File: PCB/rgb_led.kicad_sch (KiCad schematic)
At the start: 3 parts

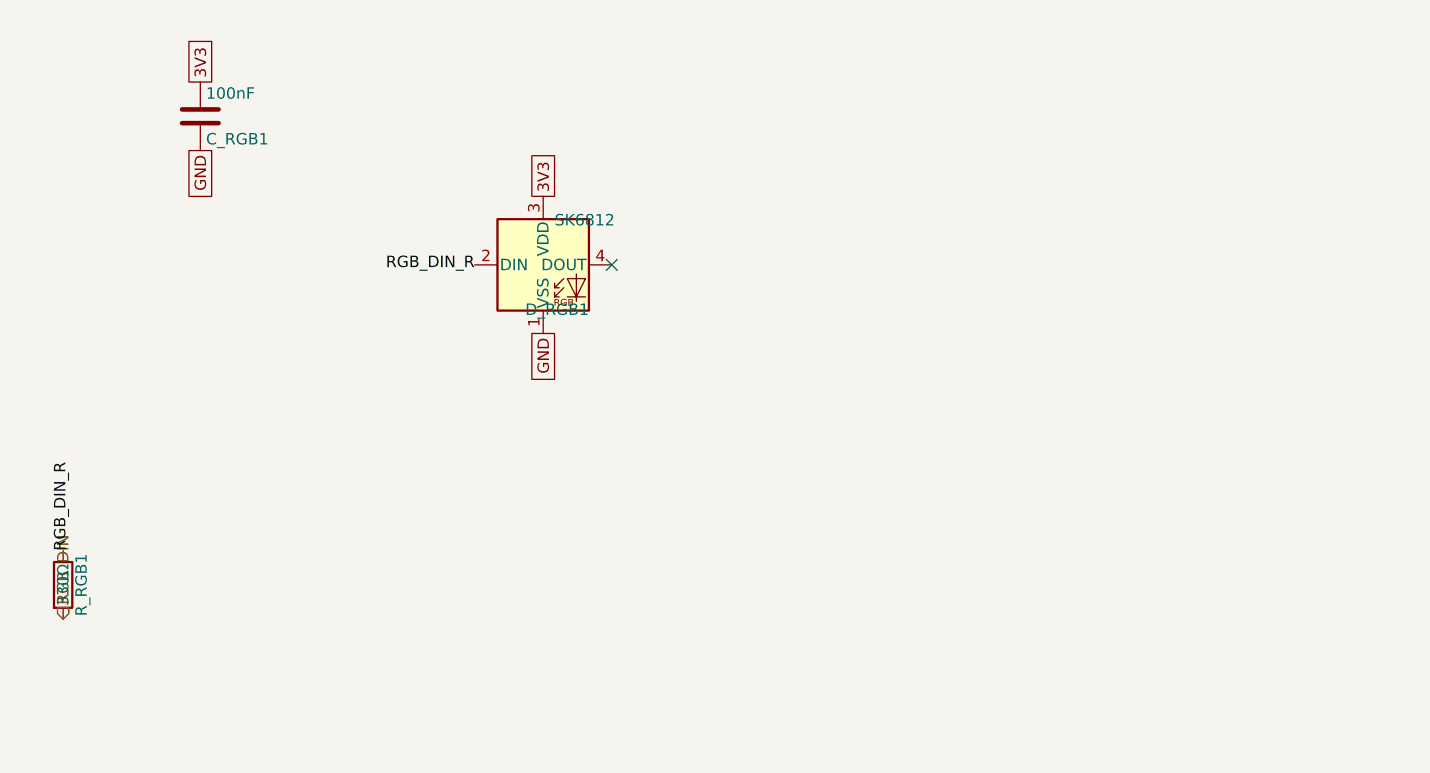
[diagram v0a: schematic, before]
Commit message: refactor: updated gulikit footprint
This updates the gulikit thumbstick footprint to be accurate.
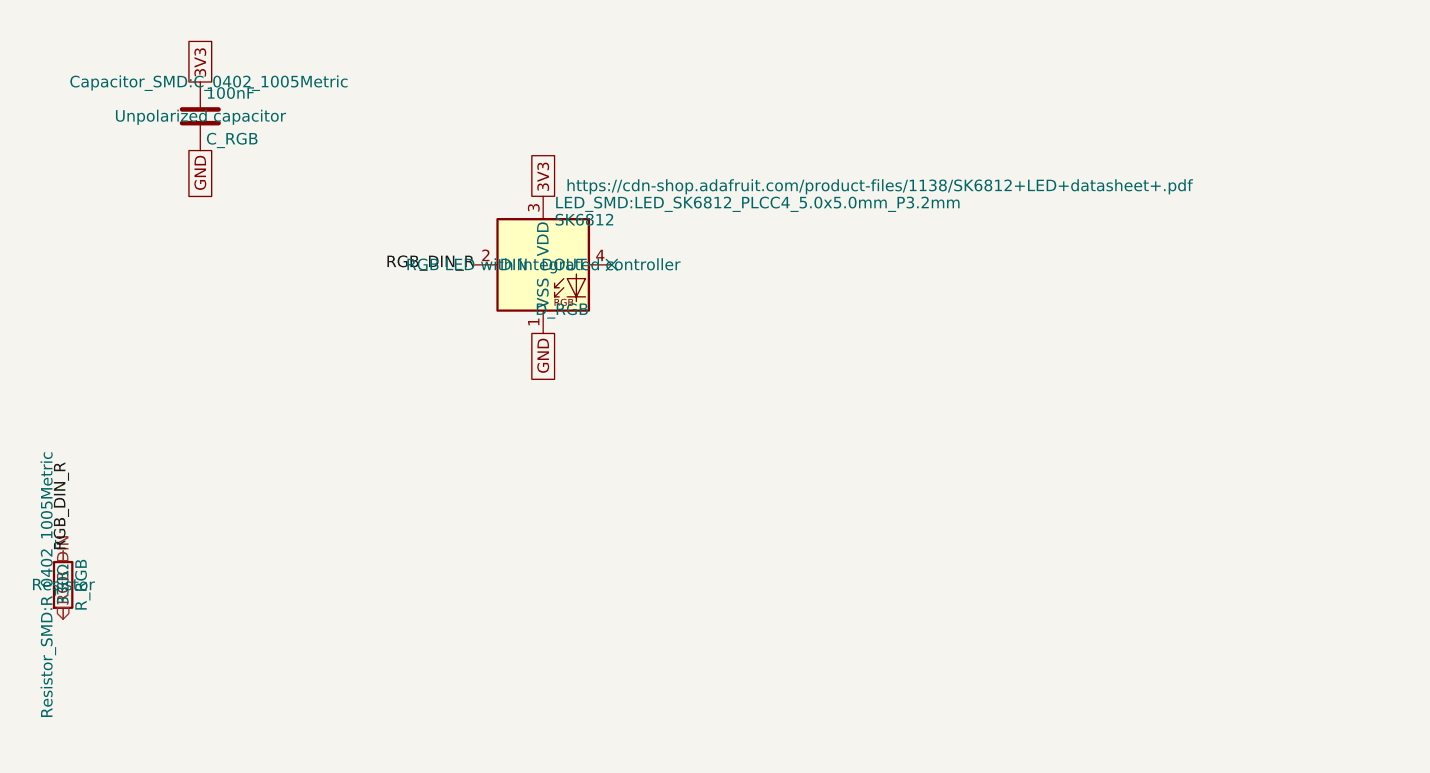
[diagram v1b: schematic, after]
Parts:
- removed C_RGB1: 100nF, Capacitor_SMD:C_0402_1005Metric, symbol Device:C
- removed D_RGB1: SK6812, LED_SMD:LED_SK6812_PLCC4_5.0x5.0mm_P3.2mm, symbol LED:SK6812
- removed R_RGB1: 330Ω, Resistor_SMD:R_0402_1005Metric, symbol Device:R
- added C_RGB: 100nF, Capacitor_SMD:C_0402_1005Metric, symbol Device:C
- added D_RGB: SK6812, LED_SMD:LED_SK6812_PLCC4_5.0x5.0mm_P3.2mm, symbol LED:SK6812
- added R_RGB: 330Ω, Resistor_SMD:R_0402_1005Metric, symbol Device:R
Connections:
- net 3V3: now also C_RGB.1, D_RGB.3 (VDD)
- net GND: now also C_RGB.2, D_RGB.1 (VSS)
- net RGB_DIN: now also R_RGB.2
- net RGB_DIN_R: now also D_RGB.2 (DIN), R_RGB.1
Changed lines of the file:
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@@
 		(dnp no)
 		(fields_autoplaced yes)
-		(property "Reference" "D_RGB1"
+		(property "Reference" "D_RGB"
 			(at 180.34 100.965 0)
 			(show_name no)
@@
 		(property "Footprint" "LED_SMD:LED_SK6812_PLCC4_5.0x5.0mm_P3.2mm"
 			(at 176.53 87.63 0)
-			(hide yes)
 			(show_name no)
 			(do_not_autoplace no)
@@
 		(property "Datasheet" "https://cdn-shop.adafruit.com/product-files/1138/SK6812+LED+datasheet+.pdf"
 			(at 177.8 85.725 0)
-			(hide yes)
 			(show_name no)
 			(do_not_autoplace no)
@@
 		(property "Description" "RGB LED with integrated controller"
 			(at 175.26 95.25 0)
-			(hide yes)
 			(show_name no)
 			(do_not_autoplace no)
@@
 		)
 		(instances
-			(project "snips_controller"
-				(path "/868f8289-8434-4465-b2f4-2accc5e40bab/735d8d44-e064-4356-9d02-a40b0078b674"
-					(reference "D_RGB1")
+			(project ""
+				(path "/d0f5b7d7-b2b6-4492-958c-e60265d3c6b4/e8a027f5-b0c3-4230-8e98-ef586f634016"
+					(reference "D_RGB")
 					(unit 1)
 				)
@@
 		(dnp no)
 		(fields_autoplaced yes)
-		(property "Reference" "C_RGB1"
+		(property "Reference" "C_RGB"
 			(at 137.795 81.28 0)
 			(show_name no)
@@
 		(property "Footprint" "Capacitor_SMD:C_0402_1005Metric"
 			(at 138.1252 74.93 0)
-			(hide yes)
 			(show_name no)
 			(do_not_autoplace no)
@@
 		(property "Datasheet" ""
 			(at 137.16 78.74 0)
-			(hide yes)
 			(show_name no)
 			(do_not_autoplace no)
@@
 		(property "Description" "Unpolarized capacitor"
 			(at 137.16 78.74 0)
-			(hide yes)
 			(show_name no)
 			(do_not_autoplace no)
@@
 		)
 		(instances
-			(project "snips_controller"
-				(path "/868f8289-8434-4465-b2f4-2accc5e40bab/735d8d44-e064-4356-9d02-a40b0078b674"
-					(reference "C_RGB1")
+			(project ""
+				(path "/d0f5b7d7-b2b6-4492-958c-e60265d3c6b4/e8a027f5-b0c3-4230-8e98-ef586f634016"
+					(reference "C_RGB")
 					(unit 1)
 				)
@@
 		(dnp no)
 		(fields_autoplaced yes)
-		(property "Reference" "R_RGB1"
+		(property "Reference" "R_RGB"
 			(at 123.952 130.81 90)
 			(show_name no)
@@
 		(property "Footprint" "Resistor_SMD:R_0402_1005Metric"
 			(at 120.142 130.81 90)
-			(hide yes)
 			(show_name no)
 			(do_not_autoplace no)
@@
 		(property "Datasheet" ""
 			(at 121.92 130.81 0)
-			(hide yes)
 			(show_name no)
 			(do_not_autoplace no)
@@
 		(property "Description" "Resistor"
 			(at 121.92 130.81 0)
-			(hide yes)
 			(show_name no)
 			(do_not_autoplace no)
@@
 		)
 		(instances
-			(project "snips_controller"
-				(path "/868f8289-8434-4465-b2f4-2accc5e40bab/735d8d44-e064-4356-9d02-a40b0078b674"
-					(reference "R_RGB1")
+			(project ""
+				(path "/d0f5b7d7-b2b6-4492-958c-e60265d3c6b4/e8a027f5-b0c3-4230-8e98-ef586f634016"
+					(reference "R_RGB")
 					(unit 1)
 				)

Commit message: layout: beginning pcb layout
This updates the schematic with a few different footprints while also starts the layout.
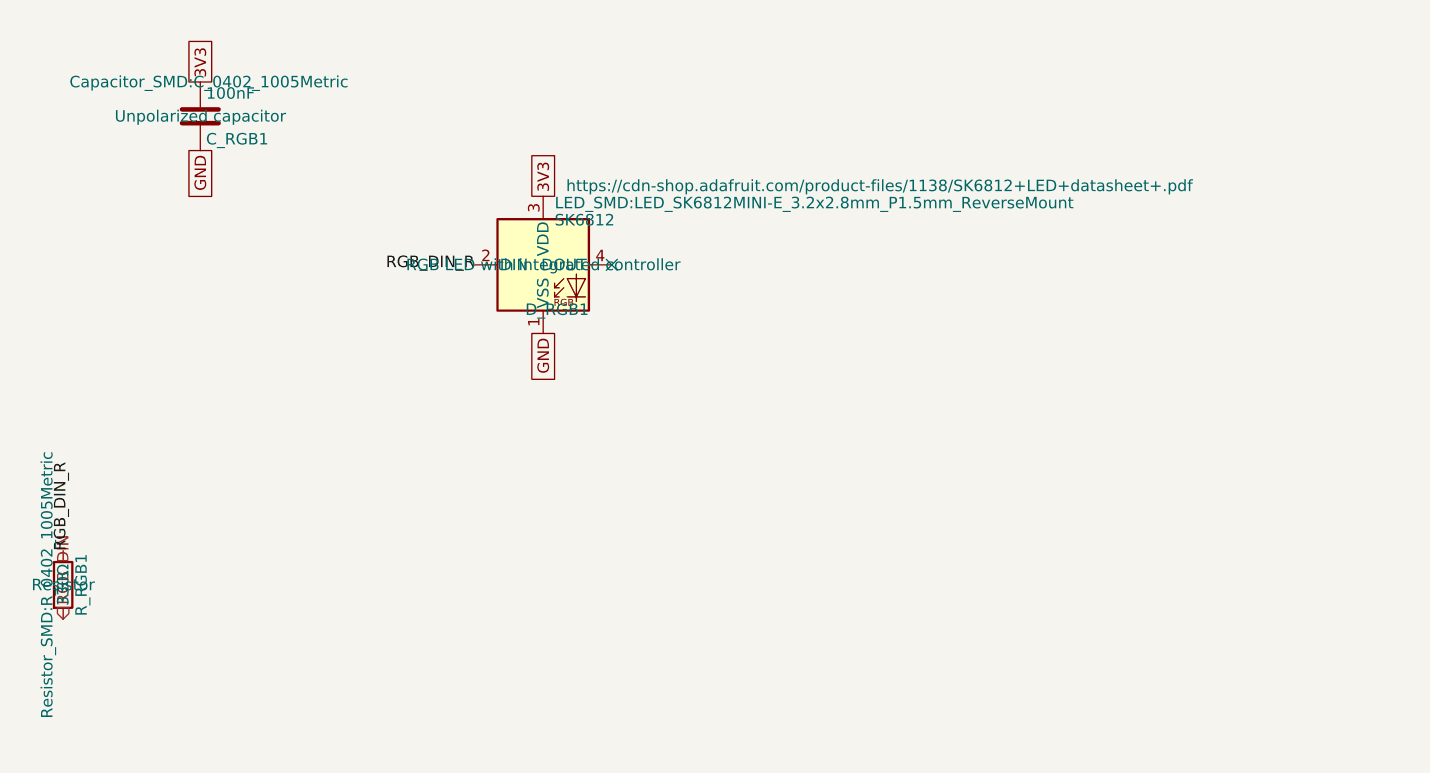
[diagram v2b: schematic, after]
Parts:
- D_RGB1: renamed from D_RGB; footprint LED_SMD:LED_SK6812_PLCC4_5.0x5.0mm_P3.2mm -> LED_SMD:LED_SK6812MINI-E_3.2x2.8mm_P1.5mm_ReverseMount
- renumbered C_RGB to C_RGB1, R_RGB to R_RGB1
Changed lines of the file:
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@@
 		(dnp no)
 		(fields_autoplaced yes)
-		(property "Reference" "D_RGB"
+		(property "Reference" "D_RGB1"
 			(at 180.34 100.965 0)
 			(show_name no)
@@
 			)
 		)
-		(property "Footprint" "LED_SMD:LED_SK6812_PLCC4_5.0x5.0mm_P3.2mm"
+		(property "Footprint" "LED_SMD:LED_SK6812MINI-E_3.2x2.8mm_P1.5mm_ReverseMount"
 			(at 176.53 87.63 0)
 			(show_name no)
@@
 		)
 		(instances
+			(project "snips_controller"
+				(path "/868f8289-8434-4465-b2f4-2accc5e40bab/e8a027f5-b0c3-4230-8e98-ef586f634016"
+					(reference "D_RGB1")
+					(unit 1)
+				)
+			)
 			(project ""
 				(path "/d0f5b7d7-b2b6-4492-958c-e60265d3c6b4/e8a027f5-b0c3-4230-8e98-ef586f634016"
@@
 		(dnp no)
 		(fields_autoplaced yes)
-		(property "Reference" "C_RGB"
+		(property "Reference" "C_RGB1"
 			(at 137.795 81.28 0)
 			(show_name no)
@@
 		)
 		(instances
+			(project "snips_controller"
+				(path "/868f8289-8434-4465-b2f4-2accc5e40bab/e8a027f5-b0c3-4230-8e98-ef586f634016"
+					(reference "C_RGB1")
+					(unit 1)
+				)
+			)
 			(project ""
 				(path "/d0f5b7d7-b2b6-4492-958c-e60265d3c6b4/e8a027f5-b0c3-4230-8e98-ef586f634016"
@@
 		(dnp no)
 		(fields_autoplaced yes)
-		(property "Reference" "R_RGB"
+		(property "Reference" "R_RGB1"
 			(at 123.952 130.81 90)
 			(show_name no)
@@
 		)
 		(instances
+			(project "snips_controller"
+				(path "/868f8289-8434-4465-b2f4-2accc5e40bab/e8a027f5-b0c3-4230-8e98-ef586f634016"
+					(reference "R_RGB1")
+					(unit 1)
+				)
+			)
 			(project ""
 				(path "/d0f5b7d7-b2b6-4492-958c-e60265d3c6b4/e8a027f5-b0c3-4230-8e98-ef586f634016"

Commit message: refactor: swap footprints and add symmetry
This updates the footprints of a couple components to be smaller and closer to what we want. It also adds two buttons to ensure left and right side symmetry.
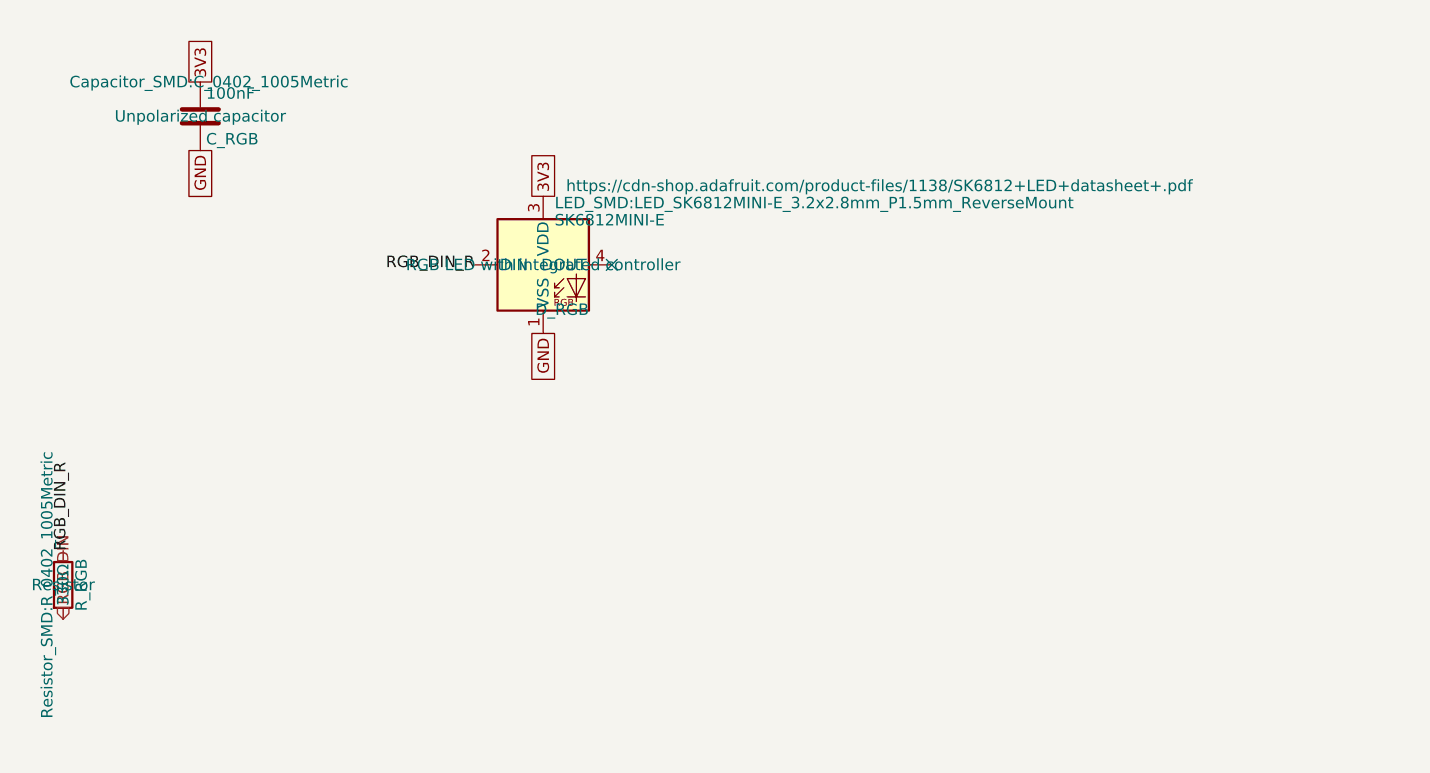
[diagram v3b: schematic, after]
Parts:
- removed C_RGB1: 100nF, Capacitor_SMD:C_0402_1005Metric, symbol Device:C
- removed D_RGB1: SK6812, LED_SMD:LED_SK6812MINI-E_3.2x2.8mm_P1.5mm_ReverseMount, symbol LED:SK6812
- removed R_RGB1: 330Ω, Resistor_SMD:R_0402_1005Metric, symbol Device:R
- added C_RGB: 100nF, Capacitor_SMD:C_0402_1005Metric, symbol Device:C
- added D_RGB: SK6812MINI-E, LED_SMD:LED_SK6812MINI-E_3.2x2.8mm_P1.5mm_ReverseMount, symbol LED:SK6812
- added R_RGB: 330Ω, Resistor_SMD:R_0402_1005Metric, symbol Device:R
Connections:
- net 3V3: now also C_RGB.1, D_RGB.3 (VDD)
- net GND: now also C_RGB.2, D_RGB.1 (VSS)
- net RGB_DIN: now also R_RGB.2
- net RGB_DIN_R: now also D_RGB.2 (DIN), R_RGB.1
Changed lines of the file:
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@@
+	)
+	(label "RGB_DIN_R"
+		(at 121.92 127 90)
+		(effects
+			(font
+				(size 1.27 1.27)
+			)
+			(justify left)
+		)
 	)
 	(label "RGB_DIN_R"
@@
 			)
 			(justify right)
-		)
-	)
-	(label "RGB_DIN_R"
-		(at 121.92 127 90)
-		(effects
-			(font
-				(size 1.27 1.27)
-			)
-			(justify left)
 		)
 	)
@@
 	(global_label "GND"
 		(shape passive)
+		(at 175.26 102.87 270)
+		(fields_autoplaced yes)
+		(effects
+			(font
+				(size 1.27 1.27)
+			)
+			(justify right)
+		)
+		(property "Intersheetrefs" "${INTERSHEET_REFS}"
+			(at 175.26 102.87 0)
+			(hide yes)
+			(show_name no)
+			(do_not_autoplace no)
+			(effects
+				(font
+					(size 1.27 1.27)
+				)
+			)
+		)
+	)
+	(global_label "GND"
+		(shape passive)
 		(at 137.16 82.55 270)
 		(fields_autoplaced yes)
@@
 		)
 	)
-	(global_label "GND"
-		(shape passive)
-		(at 175.26 102.87 270)
-		(fields_autoplaced yes)
-		(effects
-			(font
-				(size 1.27 1.27)
-			)
-			(justify right)
-		)
-		(property "Intersheetrefs" "${INTERSHEET_REFS}"
-			(at 175.26 102.87 0)
-			(hide yes)
-			(show_name no)
-			(do_not_autoplace no)
-			(effects
-				(font
-					(size 1.27 1.27)
-				)
-			)
-		)
-	)
 	(global_label "3V3"
 		(shape passive)
@@
 			)
 			(justify left)
+		)
+	)
+	(symbol
+		(lib_id "Device:C")
+		(at 137.16 78.74 0)
+		(unit 1)
+		(body_style 1)
+		(exclude_from_sim no)
+		(in_bom yes)
+		(on_board yes)
+		(in_pos_files yes)
+		(dnp no)
+		(fields_autoplaced yes)
+		(property "Reference" "C_RGB"
+			(at 137.795 81.28 0)
+			(show_name no)
+			(do_not_autoplace no)
+			(effects
+				(font
+					(size 1.27 1.27)
+				)
+				(justify left)
+			)
+		)
+		(property "Value" "100nF"
+			(at 137.795 76.2 0)
+			(show_name no)
+			(do_not_autoplace no)
+			(effects
+				(font
+					(size 1.27 1.27)
+				)
+				(justify left)
+			)
+		)
+		(property "Footprint" "Capacitor_SMD:C_0402_1005Metric"
+			(at 138.1252 74.93 0)
+			(show_name no)
+			(do_not_autoplace no)
+			(effects
+				(font
+					(size 1.27 1.27)
+				)
+			)
+		)
+		(property "Datasheet" ""
+			(at 137.16 78.74 0)
+			(show_name no)
+			(do_not_autoplace no)
+			(effects
+				(font
+					(size 1.27 1.27)
+				)
+			)
+		)
+		(property "Description" "Unpolarized capacitor"
+			(at 137.16 78.74 0)
+			(show_name no)
+			(do_not_autoplace no)
+			(effects
+				(font
+					(size 1.27 1.27)
+				)
+			)
+		)
+		(pin "1"
+		)
+		(pin "2"
+		)
+		(instances
+			(project "snips_controller"
+				(path "/f9d779c6-e1a6-4677-9004-6e9cc3d2fa8d/de2e61c0-3a94-4f0a-93aa-fbb224e49852"
+					(reference "C_RGB")
+					(unit 1)
+				)
+			)
 		)
 	)
@@
 		(dnp no)
 		(fields_autoplaced yes)
-		(property "Reference" "D_RGB1"
+		(property "Reference" "D_RGB"
 			(at 180.34 100.965 0)
 			(show_name no)
@@
 			)
 		)
-		(property "Value" "SK6812"
+		(property "Value" "SK6812MINI-E"
 			(at 176.53 89.535 0)
 			(show_name no)
@@
 		(instances
 			(project "snips_controller"
-				(path "/868f8289-8434-4465-b2f4-2accc5e40bab/e8a027f5-b0c3-4230-8e98-ef586f634016"
-					(reference "D_RGB1")
-					(unit 1)
-				)
-			)
-			(project ""
-				(path "/d0f5b7d7-b2b6-4492-958c-e60265d3c6b4/e8a027f5-b0c3-4230-8e98-ef586f634016"
+				(path "/f9d779c6-e1a6-4677-9004-6e9cc3d2fa8d/de2e61c0-3a94-4f0a-93aa-fbb224e49852"
 					(reference "D_RGB")
-					(unit 1)
-				)
-			)
-		)
-	)
-	(symbol
-		(lib_id "Device:C")
-		(at 137.16 78.74 0)
-		(unit 1)
-		(body_style 1)
-		(exclude_from_sim no)
-		(in_bom yes)
-		(on_board yes)
-		(in_pos_files yes)
-		(dnp no)
-		(fields_autoplaced yes)
-		(property "Reference" "C_RGB1"
-			(at 137.795 81.28 0)
-			(show_name no)
-			(do_not_autoplace no)
-			(effects
-				(font
-					(size 1.27 1.27)
-				)
-				(justify left)
-			)
-		)
-		(property "Value" "100nF"
-			(at 137.795 76.2 0)
-			(show_name no)
-			(do_not_autoplace no)
-			(effects
-				(font
-					(size 1.27 1.27)
-				)
-				(justify left)
-			)
-		)
-		(property "Footprint" "Capacitor_SMD:C_0402_1005Metric"
-			(at 138.1252 74.93 0)
-			(show_name no)
-			(do_not_autoplace no)
-			(effects
-				(font
-					(size 1.27 1.27)
-				)
-			)
-		)
-		(property "Datasheet" ""
-			(at 137.16 78.74 0)
-			(show_name no)
-			(do_not_autoplace no)
-			(effects
-				(font
-					(size 1.27 1.27)
-				)
-			)
-		)
-		(property "Description" "Unpolarized capacitor"
-			(at 137.16 78.74 0)
-			(show_name no)
-			(do_not_autoplace no)
-			(effects
-				(font
-					(size 1.27 1.27)
-				)
-			)
-		)
-		(pin "1"
-		)
-		(pin "2"
-		)
-		(instances
-			(project "snips_controller"
-				(path "/868f8289-8434-4465-b2f4-2accc5e40bab/e8a027f5-b0c3-4230-8e98-ef586f634016"
-					(reference "C_RGB1")
-					(unit 1)
-				)
-			)
-			(project ""
-				(path "/d0f5b7d7-b2b6-4492-958c-e60265d3c6b4/e8a027f5-b0c3-4230-8e98-ef586f634016"
-					(reference "C_RGB")
 					(unit 1)
 				)
@@
 		(dnp no)
 		(fields_autoplaced yes)
-		(property "Reference" "R_RGB1"
+		(property "Reference" "R_RGB"
 			(at 123.952 130.81 90)
 			(show_name no)
@@
 		(instances
 			(project "snips_controller"
-				(path "/868f8289-8434-4465-b2f4-2accc5e40bab/e8a027f5-b0c3-4230-8e98-ef586f634016"
-					(reference "R_RGB1")
-					(unit 1)
-				)
-			)
-			(project ""
-				(path "/d0f5b7d7-b2b6-4492-958c-e60265d3c6b4/e8a027f5-b0c3-4230-8e98-ef586f634016"
+				(path "/f9d779c6-e1a6-4677-9004-6e9cc3d2fa8d/de2e61c0-3a94-4f0a-93aa-fbb224e49852"
 					(reference "R_RGB")
 					(unit 1)
